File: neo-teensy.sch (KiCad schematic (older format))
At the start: 30 parts, among them J1 Conn_01x03_Male, J10 Conn_01x14, J11 Conn_02x04_Odd_Even, J12 Conn_01x02, J2 Conn_01x03_Male, J3 Conn_01x14_Male, J4 Conn_01x03_Male, J5 Conn_01x05_Male, J6 Conn_01x03_Male, J7 Conn_01x14_Male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

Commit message: Minor cleanup.
Signed-off-by: Aaron Williams <aaron.w2@gmail.com>
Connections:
- net labels removed: DO_R
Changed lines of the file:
@@
 	4150 5750 4600 5750
 Text Label 4300 4650 0    50   ~ 0
-DO_R
+DO
 Text Label 4300 4750 0    50   ~ 0
 IO6_H

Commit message: Updated BOM
Signed-off-by: Aaron Williams <aaron.w2@gmail.com>
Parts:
- C1, C13, C2, C4, C6, C8: MFR (none) -> Samsung; MPN (none) -> CL10B104KO8WPNC; SPN (none) -> 1276-6582-1-ND; SPR (none) -> Digikey; SPURL (none) -> -
- C10, C11, C14, C5, C7, C9: MFR (none) -> Murata Electronics; MPN (none) -> GRM21BR71A106KA73K; SPN (none) -> 490-14381-1-ND; SPR (none) -> Digikey; SPURL (none) -> -
- C12, C3: MFR (none) -> Samsung; MPN (none) -> CL10B105KA8NNNC; SPN (none) -> 1276-1184-1-ND; SPR (none) -> Digikey; SPURL (none) -> -
- D1: MFR (none) -> Worldsemi; MPN (none) -> WS2813-Mini(WS2813-3535); SPN (none) -> -; SPR (none) -> -; SPURL (none) -> -
- FID1, FID2, J10, J11, J12, J3, J5, J7, J8, J9: MFR (none) -> -; MPN (none) -> -; SPN (none) -> -; SPR (none) -> -; SPURL (none) -> -
- J1, J2, J4, J6: MFR (none) -> JST Sales America Inc.; MPN (none) -> BM03B-SRSS-TBT(LF)(SN); SPN (none) -> 455-2957-1-ND; SPR (none) -> Digikey; SPURL (none) -> -
- U1: MFR (none) -> Texas Instruments; MPN SN74AHCT125N -> SN74AHCT125RGYR; SPN (none) -> 296-13910-1-ND; SPR (none) -> Digikey; SPURL (none) -> -

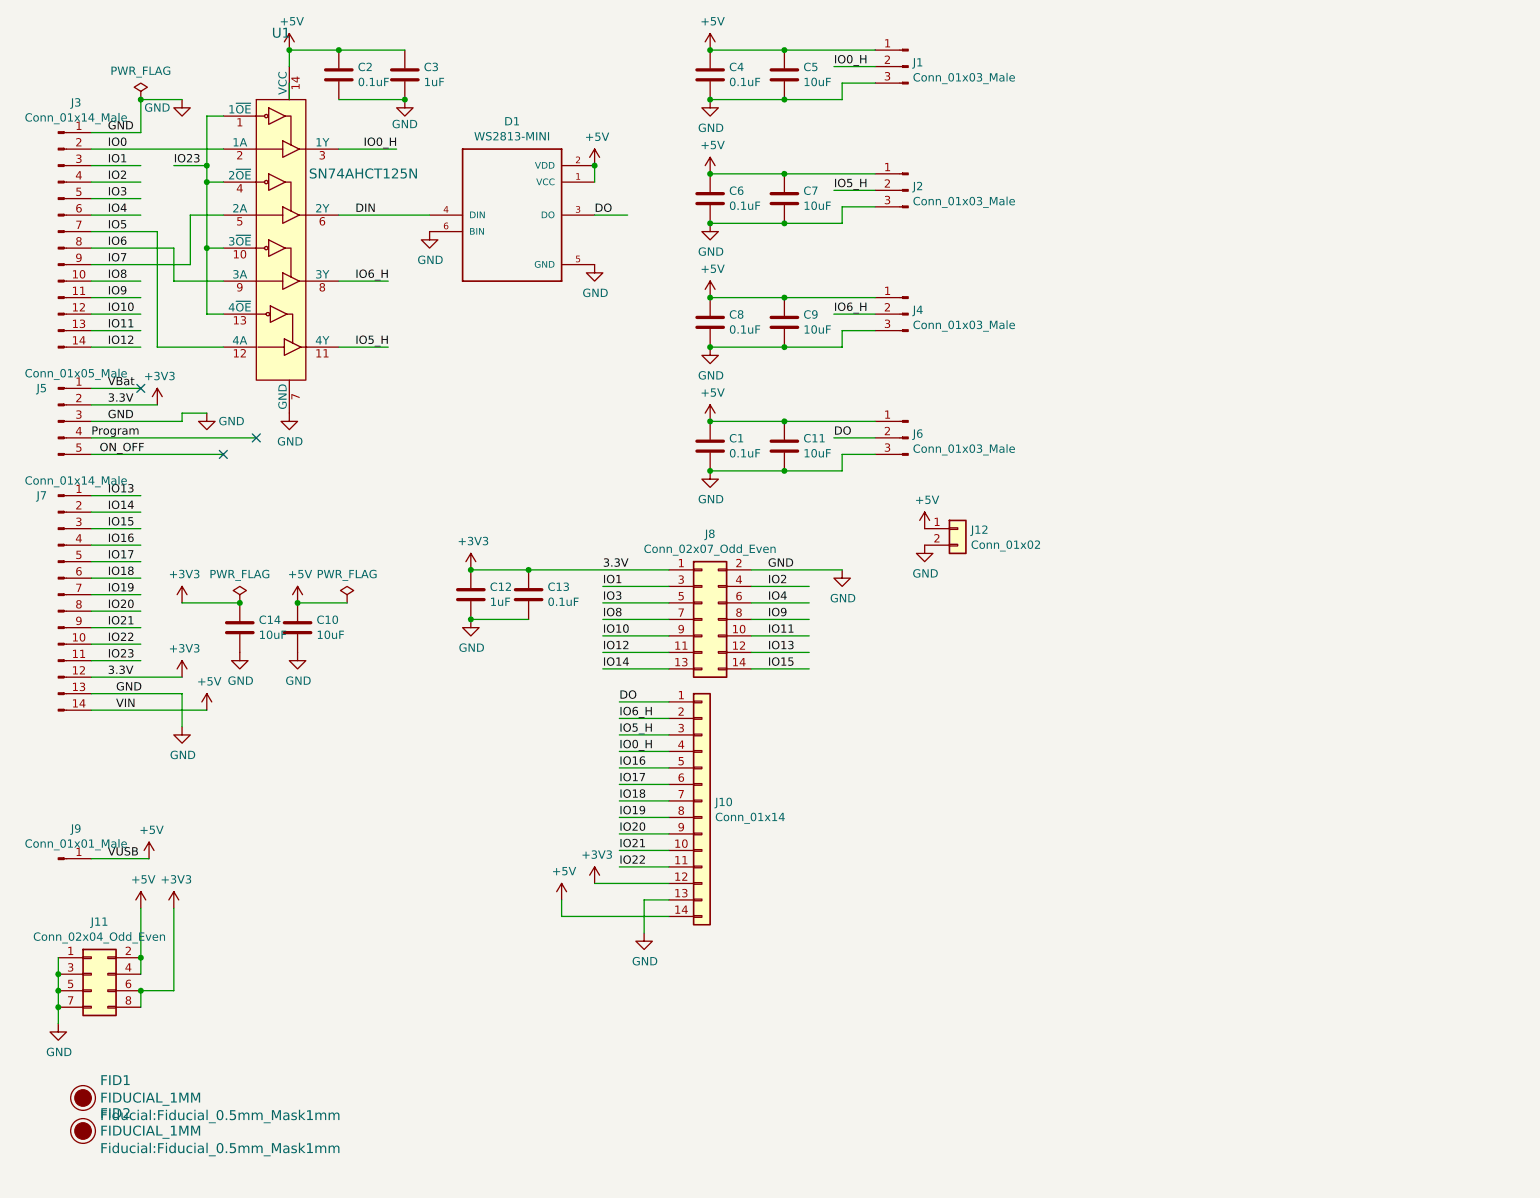
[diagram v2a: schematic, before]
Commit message: Removed connectors and added 12V boost
Version 3.1.0

Signed-off-by: Aaron Williams <aaron.w2@gmail.com>
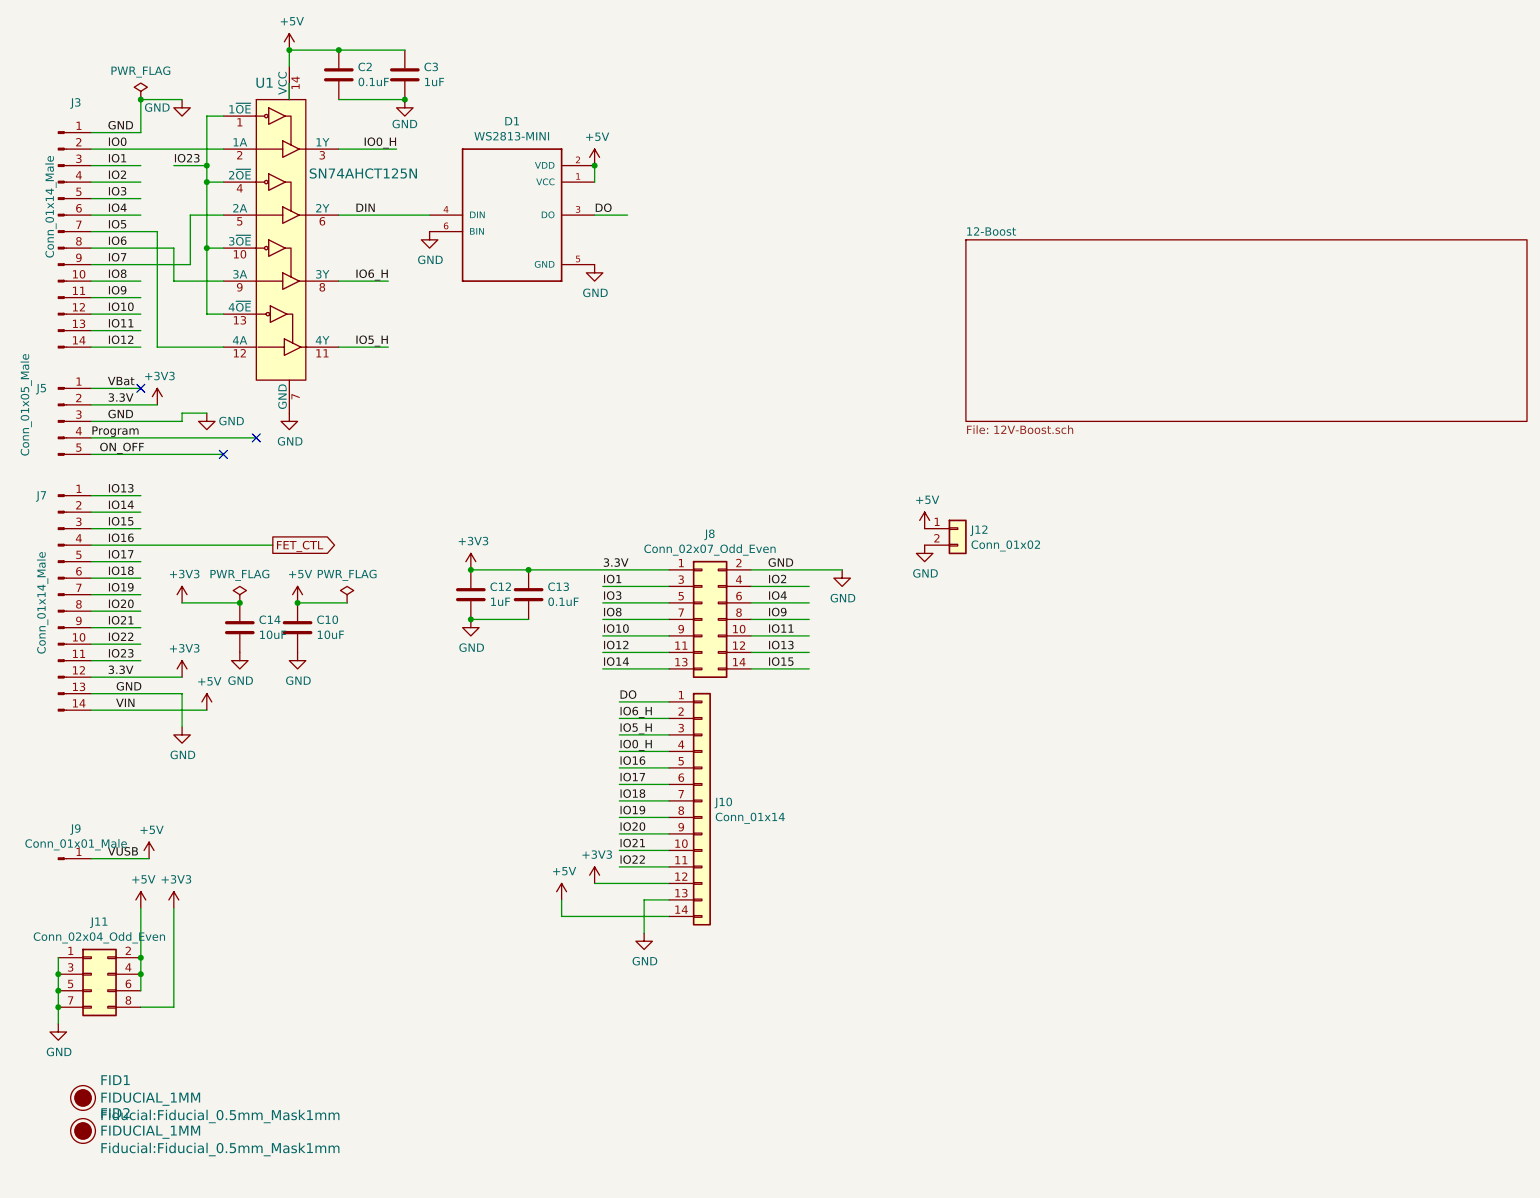
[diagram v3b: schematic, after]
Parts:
- removed C1, C4, C6, C8: 0.1uF, Capacitor_SMD:C_0603_1608Metric, symbol Device:C
- removed C11, C5, C7, C9: 10uF, Capacitor_SMD:C_0805_2012Metric, symbol Device:C
- removed J1, J2, J4, J6: Conn_01x03_Male, Connector_JST:JST_SH_BM03B-SRSS-TB_1x03-1MP_P1.00mm_Vertical, symbol Connector:Conn_01x03_Male
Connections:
- net labels added: FET_CTL
- wire segments 136 -> 108

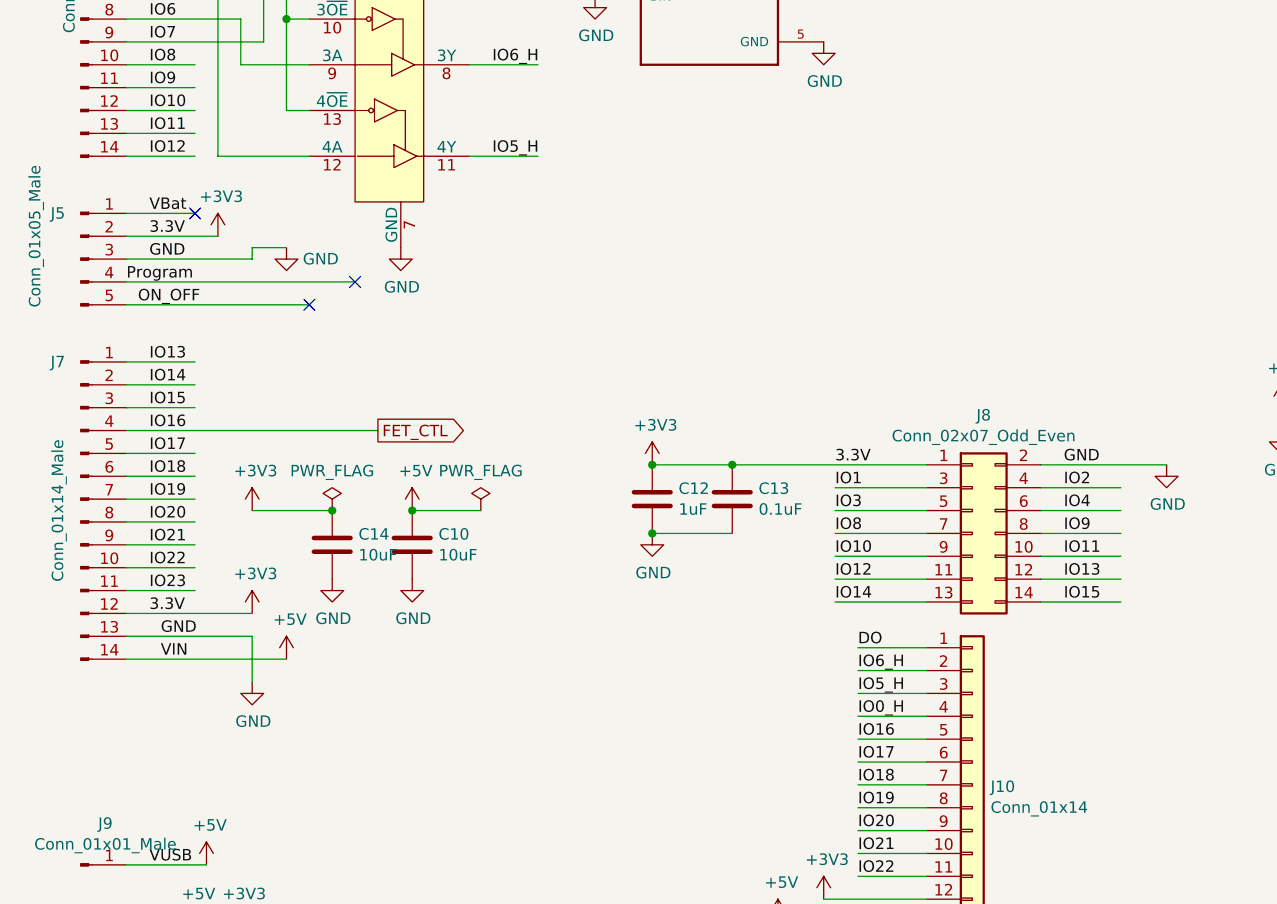
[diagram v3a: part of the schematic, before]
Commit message: Fixed GPIO 13, GPIO 16 and GPIO 17 for the fan control.
Signed-off-by: Aaron Williams <aaron.w2@gmail.com>
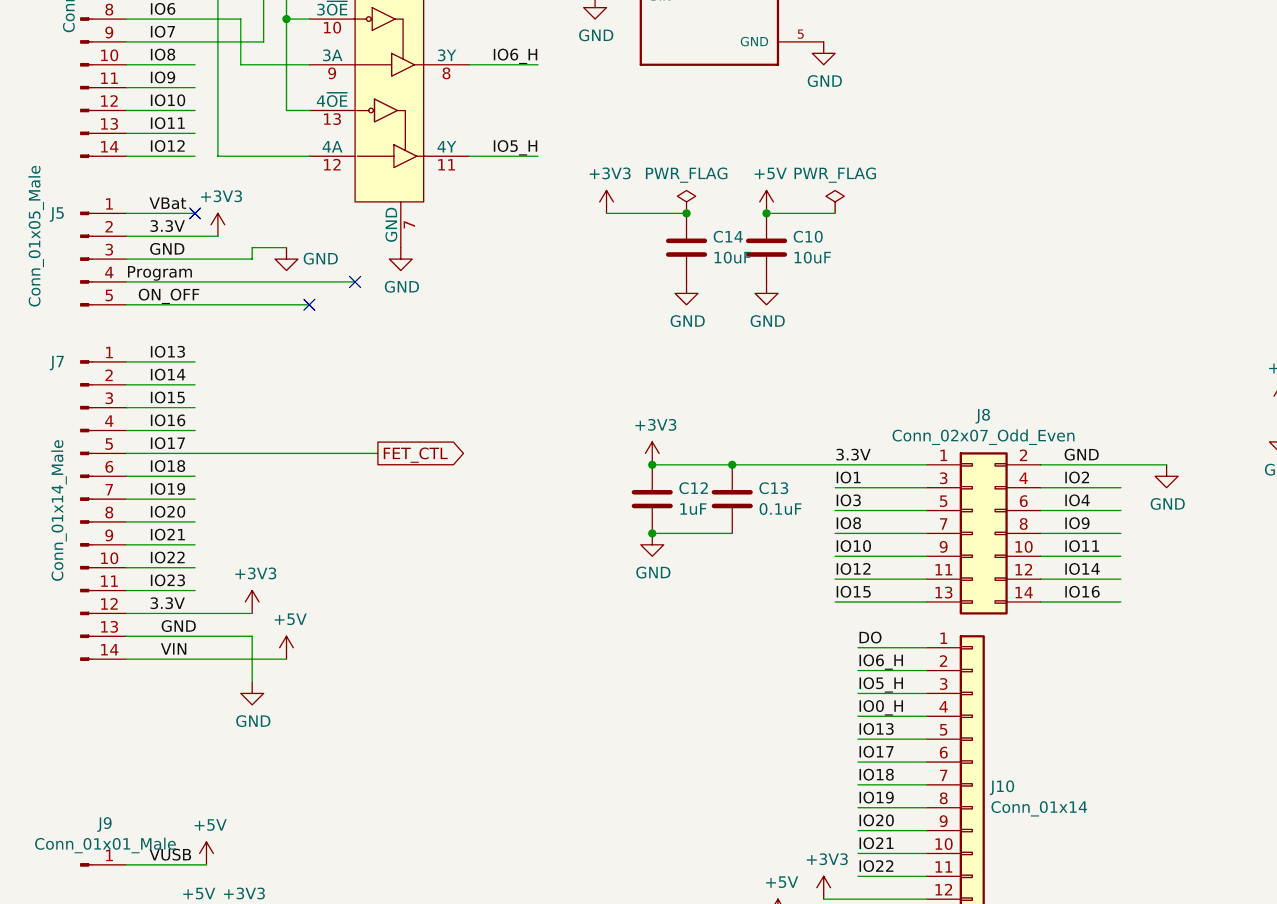
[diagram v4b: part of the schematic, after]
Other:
- moved on the sheet: C10, C14
